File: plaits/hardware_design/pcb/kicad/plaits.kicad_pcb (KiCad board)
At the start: 2 copper layers, 59 x 106.7 mm, 162 parts, among them IC1 R-78E3.3-0.5, IC2 TLC59281DBQ, IC3 LD2981ABU33, IC4 STM32F373CCT6, IC5 PCM5100APW, IC6 MCP6004, IC7 MCP6004, IC8 TL072PW, IC9 LM4040B10, J1 PJ301_THONKICONN6, J10 PJ301_THONKICONN6, J2 PJ301_THONKICONN6, J3 PJ301_THONKICONN6, J4 PJ301_THONKICONN6, J5 PJ301_THONKICONN6, J6 PJ301_THONKICONN6, J7 PJ301_THONKICONN6, J8 PJ301_THONKICONN6, J9 PJ301_THONKICONN6, Q1 8MHz

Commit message: update pcb from schematic (no change but it removed some logos)
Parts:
- removed U$1: , plaits:FCC_MEDIUM
- removed U$2: , plaits:ROHS_BIG
- removed U$3: , plaits:CE_MEDIUM
- JP5: value (none) -> M02PTH
- JP6: value (none) -> M04PTH
- L2, L3, L4, L5: value (none) -> WE-CBF_0603
- SW1, SW2: value (none) -> TAC_SWITCHPTH
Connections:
- net FM_IN renamed Net-(C57-Pad1)
- net GATE_IN renamed Net-(C61-Pad1)
- net GATE_IN1 renamed Net-(C59-Pad1)
- net HARMONICS_IN renamed Net-(C58-Pad1)
- net MODEL_IN renamed Net-(C55-Pad1)
- net MORPH_IN renamed Net-(C54-Pad1)
- net RESET renamed /plaits_2/RESET
- net RX renamed /plaits_2/RX
- net SWCLK renamed /plaits_2/SWCLK
- net SWDIO renamed /plaits_2/SWDIO
- net TX renamed /plaits_2/TX
- net V_OCT_IN renamed Net-(C60-Pad1)
- IC2 pad 22: (no net) -> unconnected-(IC2-Pad22)
- IC4 pad 2: (no net) -> unconnected-(IC4-Pad2)
- IC4 pad 3: (no net) -> unconnected-(IC4-Pad3)
- IC4 pad 38: (no net) -> unconnected-(IC4-Pad38)
- IC4 pad 39: (no net) -> unconnected-(IC4-Pad39)
- IC4 pad 4: (no net) -> unconnected-(IC4-Pad4)
- IC4 pad 40: (no net) -> unconnected-(IC4-Pad40)
- IC4 pad 41: (no net) -> unconnected-(IC4-Pad41)
- J10 pad P2: (no net) -> unconnected-(J10-PadP2)
- J9 pad P2: (no net) -> unconnected-(J9-PadP2)

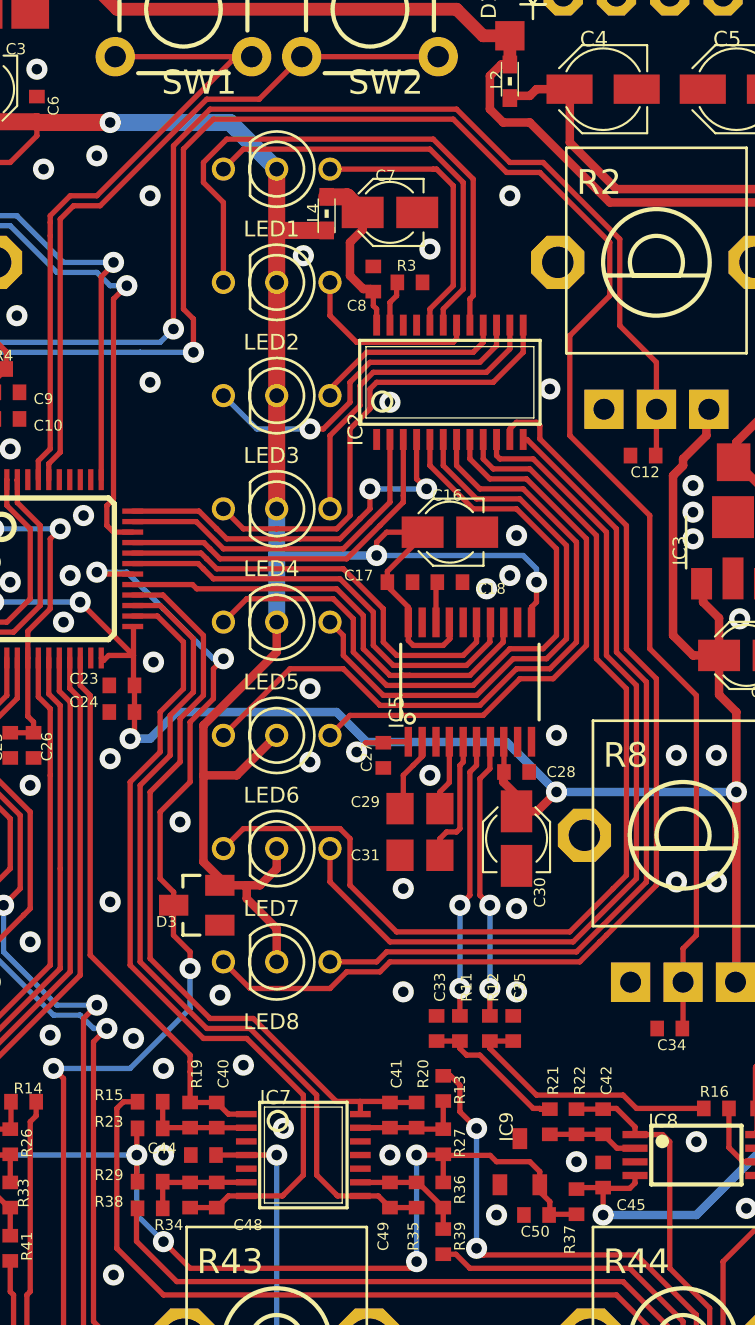
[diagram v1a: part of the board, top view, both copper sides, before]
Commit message: plaits larger LED pads
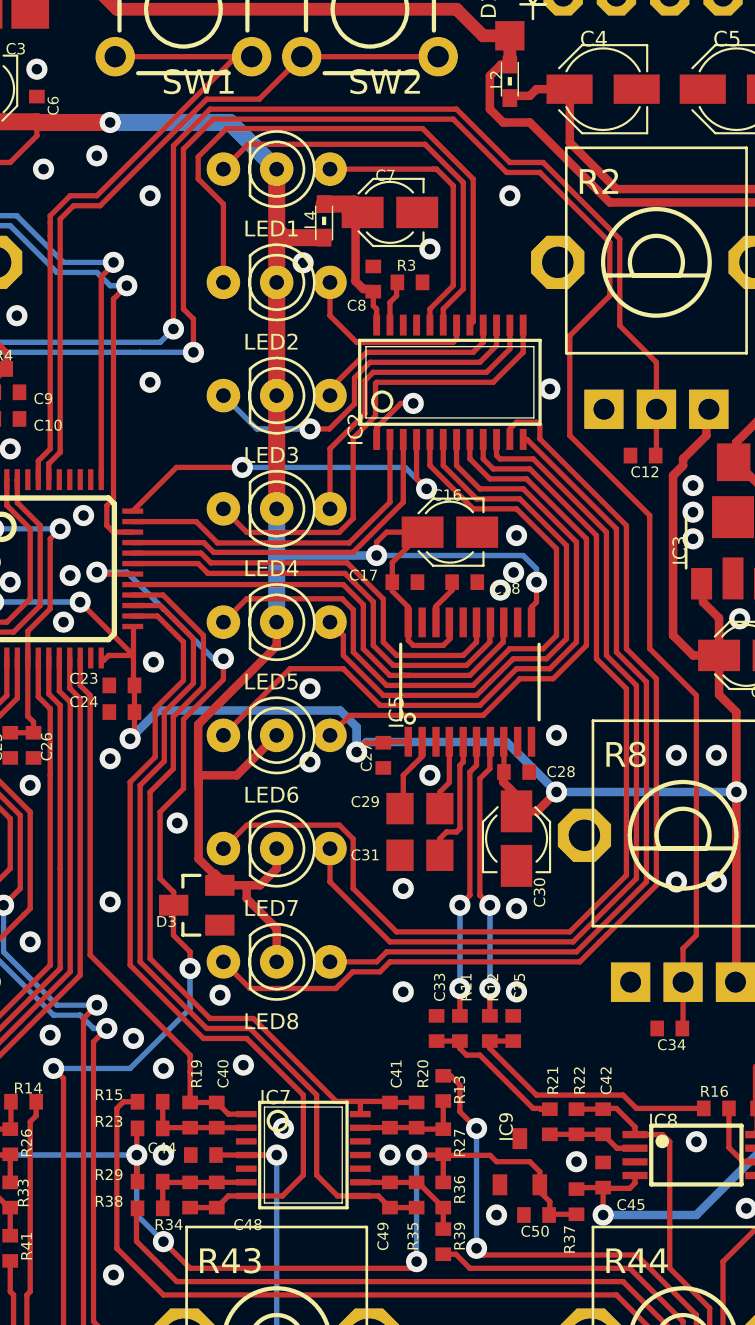
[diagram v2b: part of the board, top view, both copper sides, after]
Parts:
- moved C18 0.70 mm to (157.4, 85.3)
- moved L4 0.37 mm to (150.8, 68.2)
- moved C17 0.24 mm to (154.6, 85.3)
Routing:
- net GND: track 0.38 -> 3.17 mm
- net Net-(IC2-Pad17): track 27.2 -> 28.2 mm
- net LEDS_SS: track 18.7 -> 17.8 mm

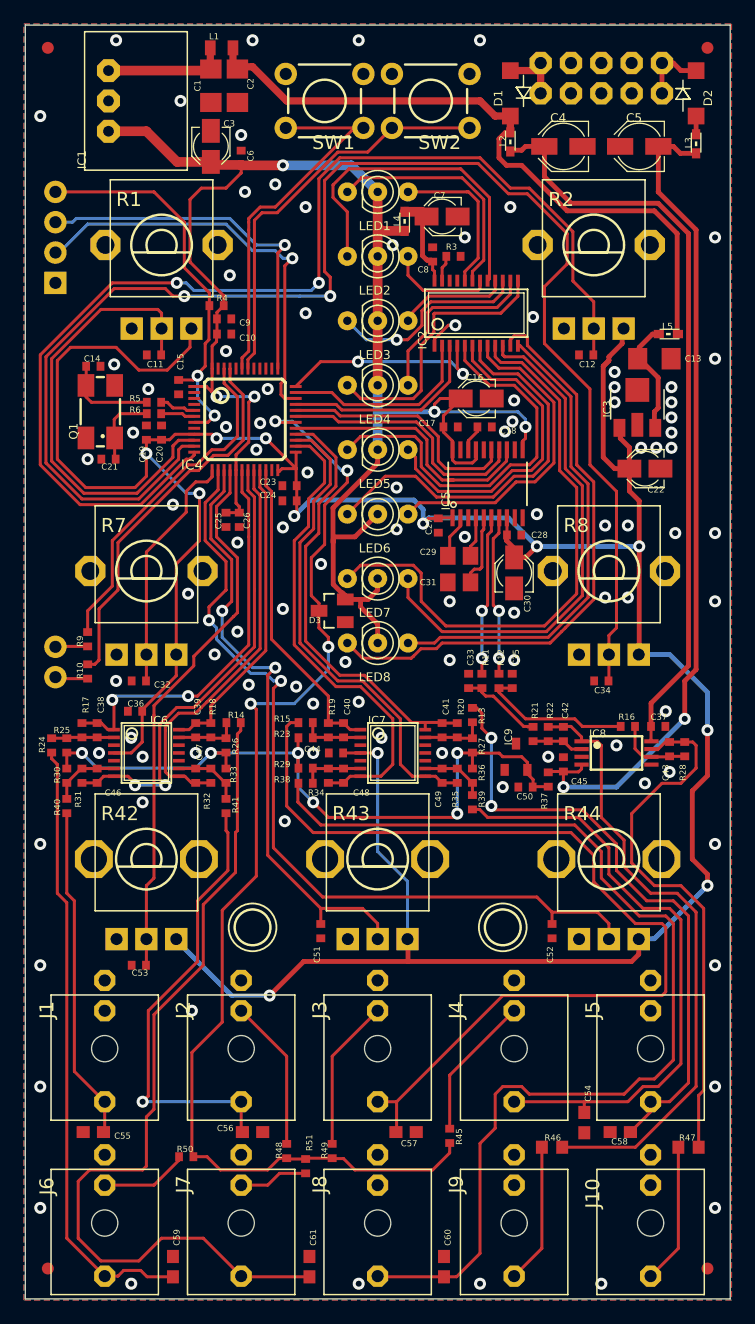
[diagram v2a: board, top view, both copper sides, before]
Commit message: plaits clean up traces + vias
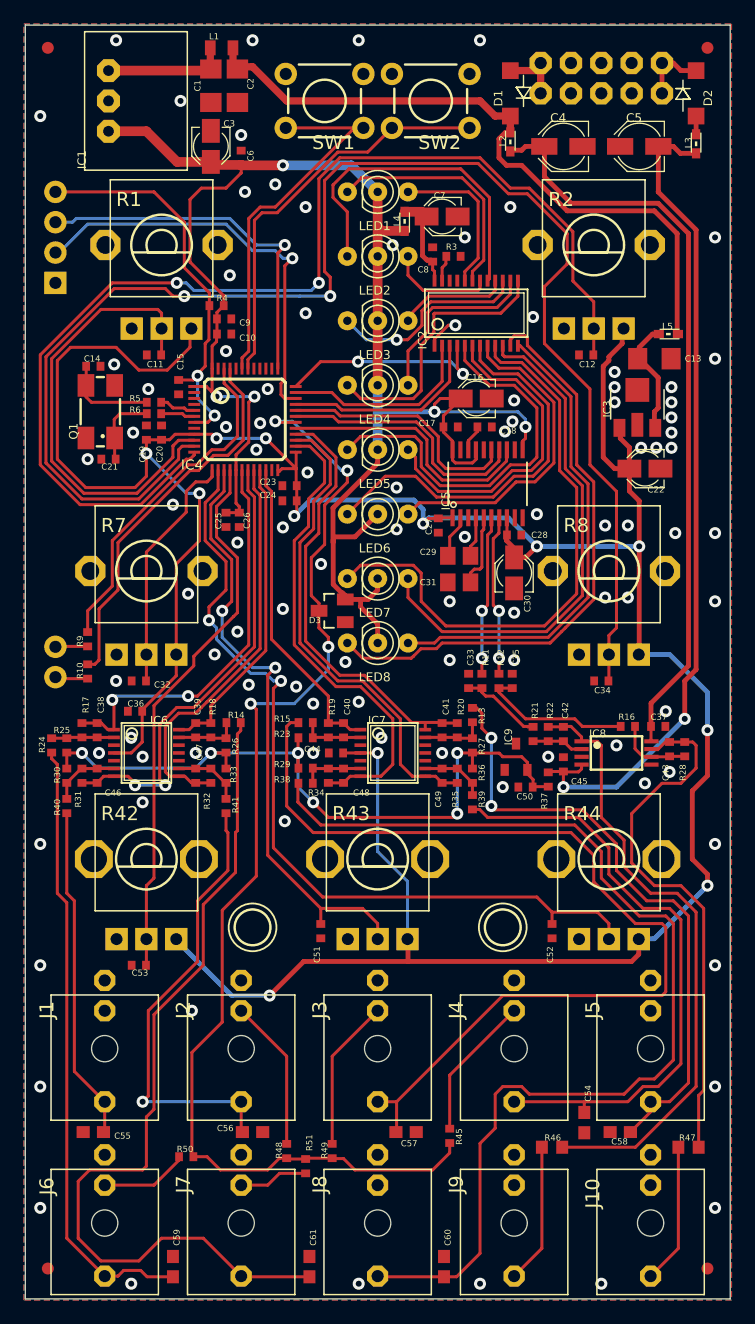
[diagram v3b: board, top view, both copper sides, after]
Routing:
- net +3V3_A: track 260.3 -> 257.6 mm
- net +3V3: track 144.9 -> 143.4 mm
- net Net-(C2-Pad1): track 56.7 -> 55.8 mm
- net SW_1: track 32.1 -> 31.3 mm
- net AREF_-10: track 60.6 -> 59.8 mm
- net Net-(D1-PadA): track 5.08 -> 4.44 mm
- net DAC_BCK: track 22.8 -> 22.3 mm

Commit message: plaits resized panasonic A -> B caps
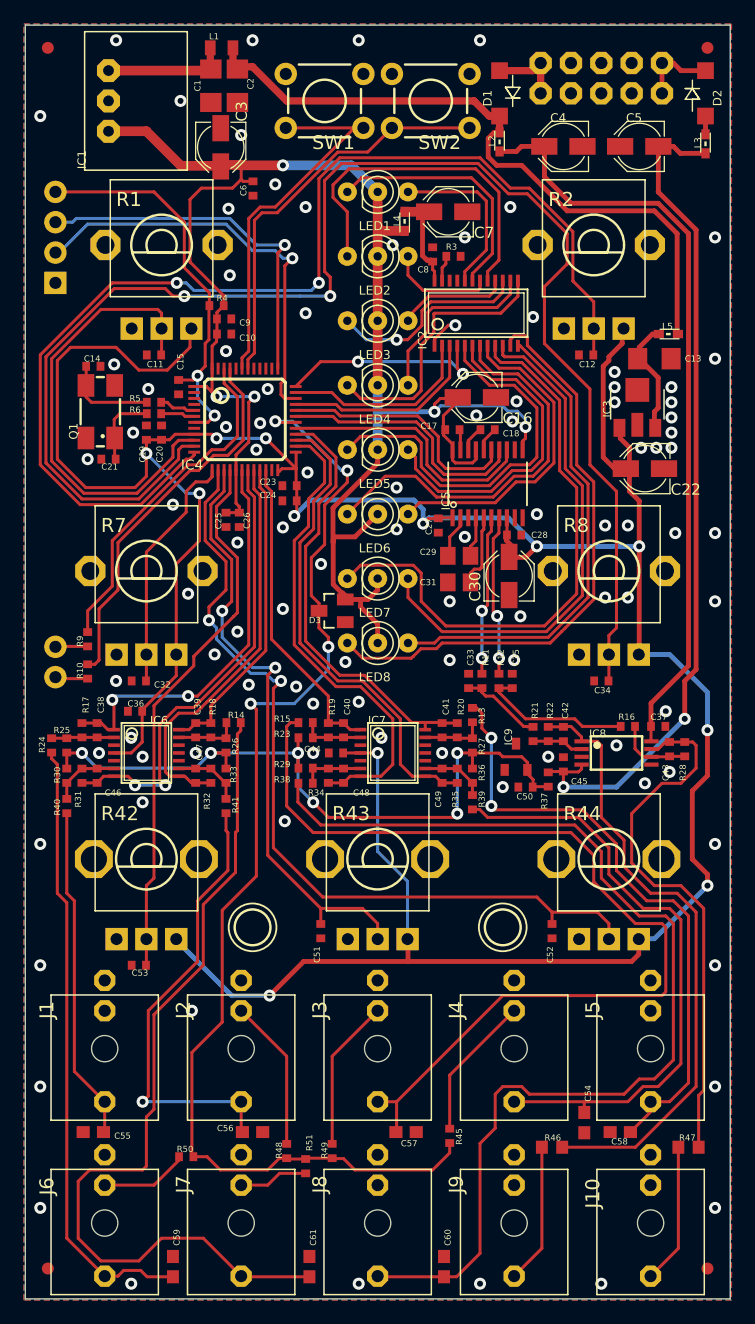
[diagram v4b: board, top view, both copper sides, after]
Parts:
- C16, C22, C3, C30, C7: footprint plaits:PANASONIC_A -> plaits:PANASONIC_B
- moved C6 2.76 mm to (138.1, 65.3), turned to -90 degrees
- moved D1 0.90 mm to (158.7, 57.4)
- moved L2 0.90 mm to (158.7, 61.3)
- moved C3 0.83 mm to (135.4, 61.9)
- moved D2 0.79 mm to (175.9, 57.4)
- moved L3 0.79 mm to (175.9, 61.5)
- moved C7 0.65 mm to (154.4, 67.3)
- moved C30 0.49 mm to (159.5, 97.8)
- moved C18 0.34 mm to (157.7, 85.5)
- moved C17 0.28 mm to (154.8, 85.5)
- moved C16 0.10 mm to (156.8, 82.8)
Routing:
- net GND: track 2.79 -> 6.47 mm
- net Net-(D1-PadA): track 4.44 -> 6.25 mm
- net +3V3: track 143.4 -> 144.9 mm
- net Net-(IC2-Pad17): track 28.2 -> 29.6 mm
- net Net-(IC2-Pad19): track 19.9 -> 20.9 mm
- net VCC: track 63.3 -> 64.4 mm
- net Net-(IC2-Pad20): track 13.3 -> 14.3 mm
- net Net-(D2-PadC): track 5.66 -> 6.45 mm
- net VEE: track 70.0 -> 70.8 mm
- net Net-(C7-Pad+): track 7.66 -> 7.10 mm

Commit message: plaits tweaks
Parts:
- moved C3 0.34 mm to (135.6, 61.7), turned to 180 degrees
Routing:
- net GND: vias 99 -> 100
